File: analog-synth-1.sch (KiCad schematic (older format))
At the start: 49 parts, among them J1 CONN_02X08, J2 CONN_02X03, J3 CONN_02X02, Q1 2N3904, Q2 2N3904, Q3 2N3904, Q4 2N3906, Q5 2N3904, U1 LM741, U2 LM741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

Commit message: Change vco tuning system
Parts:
- added R17: 50k, symbol R
- added R6: 100k, symbol R
- RV3, RV4: value 100k -> 10k
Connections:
- wire segments 157 -> 158
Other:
- note removed: "Note: RV4's value\nshould be about\nhalf RV3's value."

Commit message: Move some wires around
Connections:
- wire segments 158 -> 204
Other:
- moved on the sheet: R6, RV3, RV4

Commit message: Add footprints and fix pin header orientation
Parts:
- added R7: 1k, Resistors_THT:R_Axial_DIN0207_L6.3mm_D2.5mm_P10.16mm_Horizontal, symbol R
- C1, C10, C11, C15, C2, C3, C4, C6, C7, C8: footprint (none) -> Capacitors_THT:C_Disc_D5.0mm_W2.5mm_P2.50mm
- C12, C13, C14: footprint (none) -> Capacitors_THT:CP_Radial_D6.3mm_P2.50mm
- C5: footprint (none) -> Capacitors_THT:C_Disc_D3.8mm_W2.6mm_P2.50mm
- C9: footprint (none) -> Capacitors_THT:C_Rect_L7.0mm_W3.5mm_P2.50mm_P5.00mm
- J1: footprint (none) -> Pin_Headers:Pin_Header_Straight_2x08_Pitch2.54mm
- J2: footprint (none) -> Pin_Headers:Pin_Header_Straight_2x03_Pitch2.54mm
- J3: footprint (none) -> Pin_Headers:Pin_Header_Straight_2x02_Pitch2.54mm
- Q1, Q2, Q3, Q4, Q5: footprint TO_SOT_Packages_THT:TO-92_Molded_Narrow -> TO_SOT_Packages_THT:TO-92_Inline_Wide
- R1, R2, R3, R4, R5: footprint (none) -> Resistors_THT:R_Axial_DIN0207_L6.3mm_D2.5mm_P10.16mm_Horizontal
- R10: renamed from R8; footprint (none) -> Resistors_THT:R_Axial_DIN0207_L6.3mm_D2.5mm_P10.16mm_Horizontal
- R11: renamed from R10; footprint (none) -> Resistors_THT:R_Axial_DIN0207_L6.3mm_D2.5mm_P10.16mm_Horizontal
- R12: renamed from R11; footprint (none) -> Resistors_THT:R_Axial_DIN0207_L6.3mm_D2.5mm_P10.16mm_Horizontal
- R13: renamed from R17; footprint (none) -> Resistors_THT:R_Axial_DIN0207_L6.3mm_D2.5mm_P10.16mm_Horizontal
- R14: renamed from R12; footprint (none) -> Resistors_THT:R_Axial_DIN0207_L6.3mm_D2.5mm_P10.16mm_Horizontal
- R15: renamed from R13; footprint (none) -> Resistors_THT:R_Axial_DIN0207_L6.3mm_D2.5mm_P10.16mm_Horizontal
- R16: renamed from R14; footprint (none) -> Resistors_THT:R_Axial_DIN0207_L6.3mm_D2.5mm_P10.16mm_Horizontal
- R17: renamed from R15; footprint (none) -> Resistors_THT:R_Axial_DIN0207_L6.3mm_D2.5mm_P10.16mm_Horizontal
- R18: renamed from R16; footprint (none) -> Resistors_THT:R_Axial_DIN0207_L6.3mm_D2.5mm_P10.16mm_Horizontal
- R6: renamed from R7; footprint (none) -> Resistors_THT:R_Axial_DIN0207_L6.3mm_D2.5mm_P10.16mm_Horizontal
- R8: renamed from R9; footprint (none) -> Resistors_THT:R_Axial_DIN0207_L6.3mm_D2.5mm_P10.16mm_Horizontal
- R9: renamed from R6; footprint (none) -> Resistors_THT:R_Axial_DIN0207_L6.3mm_D2.5mm_P10.16mm_Horizontal
- RV1, RV2, RV3, RV4: footprint (none) -> Potentiometers:Potentiometer_Trimmer_Bourns_3296Y
- U1, U2, U3, U4, U5, U6, U7: footprint (none) -> Housings_DIP:DIP-8_W7.62mm
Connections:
- wire segments 204 -> 158
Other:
- moved on the sheet: RV3

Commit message: Change trimmer descriptions and plot pdf
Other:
- note added: "RV1 is exponential product control.\nRV2 is product control.\nRV3 and RV4 are sum controls."
- note removed: "RV3 and RV4 are to try\nto compensate for C9's\nvalue."
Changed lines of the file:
@@
 Text Notes 1200 4500 0    60   ~ 0
 C9's value has a drastic\neffect on the VCO's frequency.
-Text Notes 1000 7350 0    60   ~ 0
-RV3 and RV4 are to try\nto compensate for C9's\nvalue.
 Wire Wire Line
 	2700 5800 2850 5800
@@
 Wire Wire Line
 	1500 4900 1500 5050
+Text Notes 3100 3800 0    60   ~ 0
+RV1 is exponential product control.\nRV2 is product control.\nRV3 and RV4 are sum controls.
 $EndSCHEMATC

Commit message: Use PJ301M-12 3.3mm jacks
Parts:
- removed J2: CONN_02X03, Pin_Headers:Pin_Header_Straight_2x03_Pitch2.54mm, symbol CONN_02X03
- removed J3: CONN_02X02, Pin_Headers:Pin_Header_Straight_2x02_Pitch2.54mm, symbol CONN_02X02
- removed R4, R6: 100k, Resistors_THT:R_Axial_DIN0207_L6.3mm_D2.5mm_P10.16mm_Horizontal, symbol R
- added J2, J3, J4: PJ301M-12, Eurocad:PJ301M-12, symbol PJ301M-12
- added RV5: POT, symbol POT
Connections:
- net labels removed: CV2, CV3
- wire segments 158 -> 156
- no-connect marks 14 -> 16
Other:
- note added: "Pitch control pot."
- moved on the sheet: C11, C12, C13, C14, C8, U4, U7

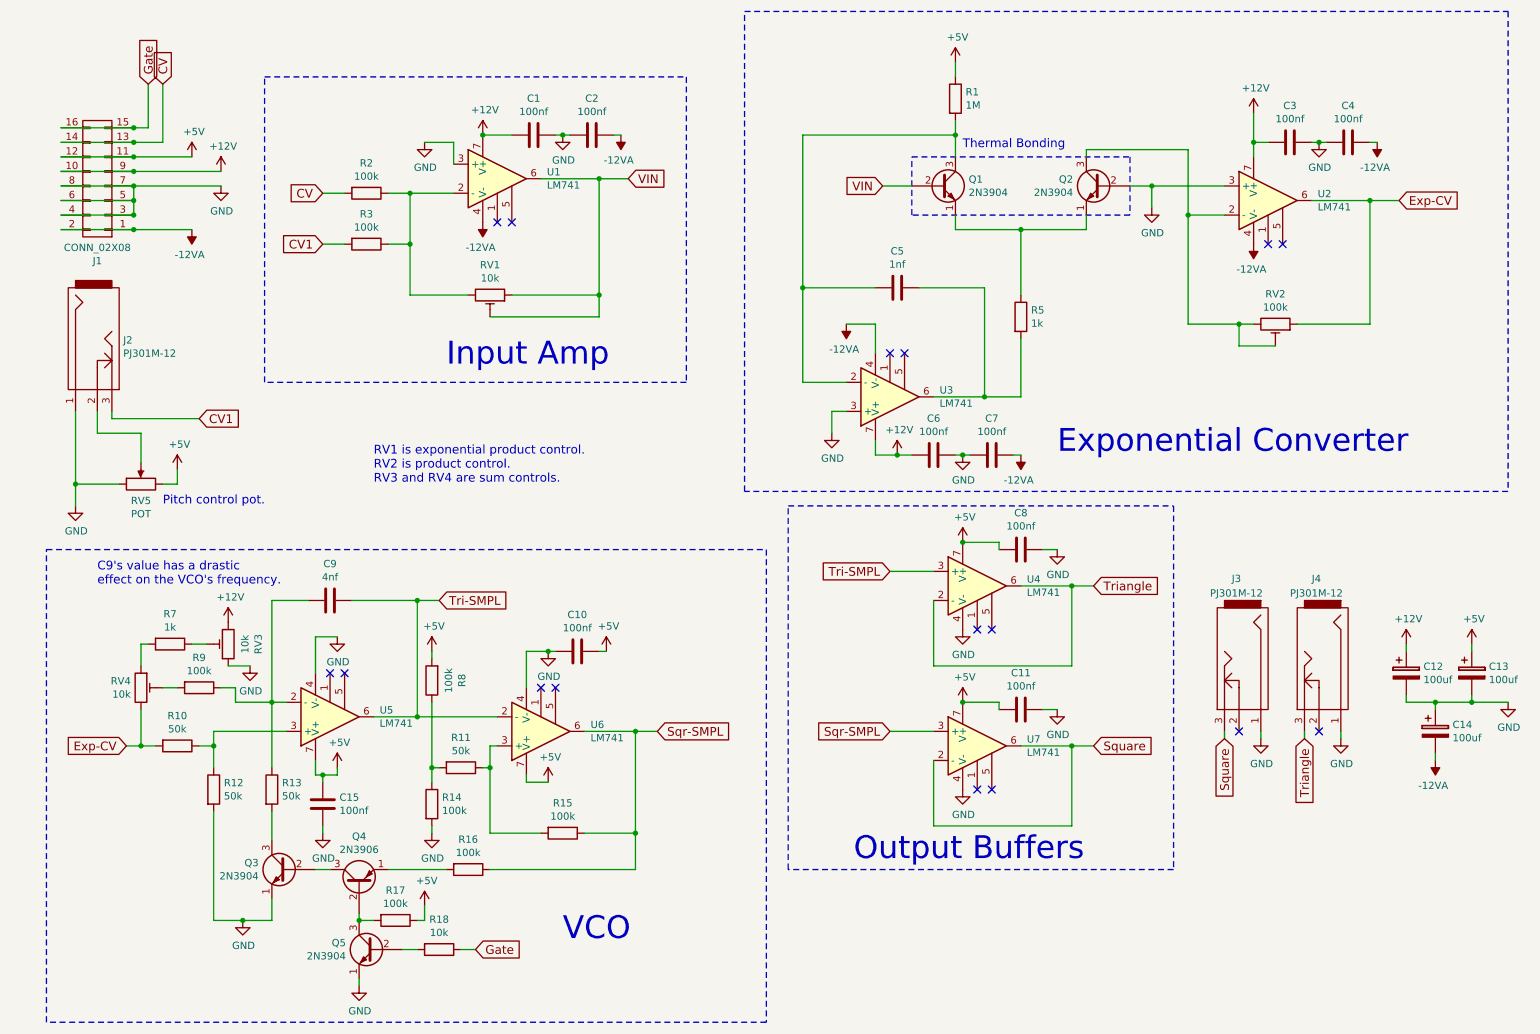
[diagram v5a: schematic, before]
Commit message: Update schematic libs, add Gate jack
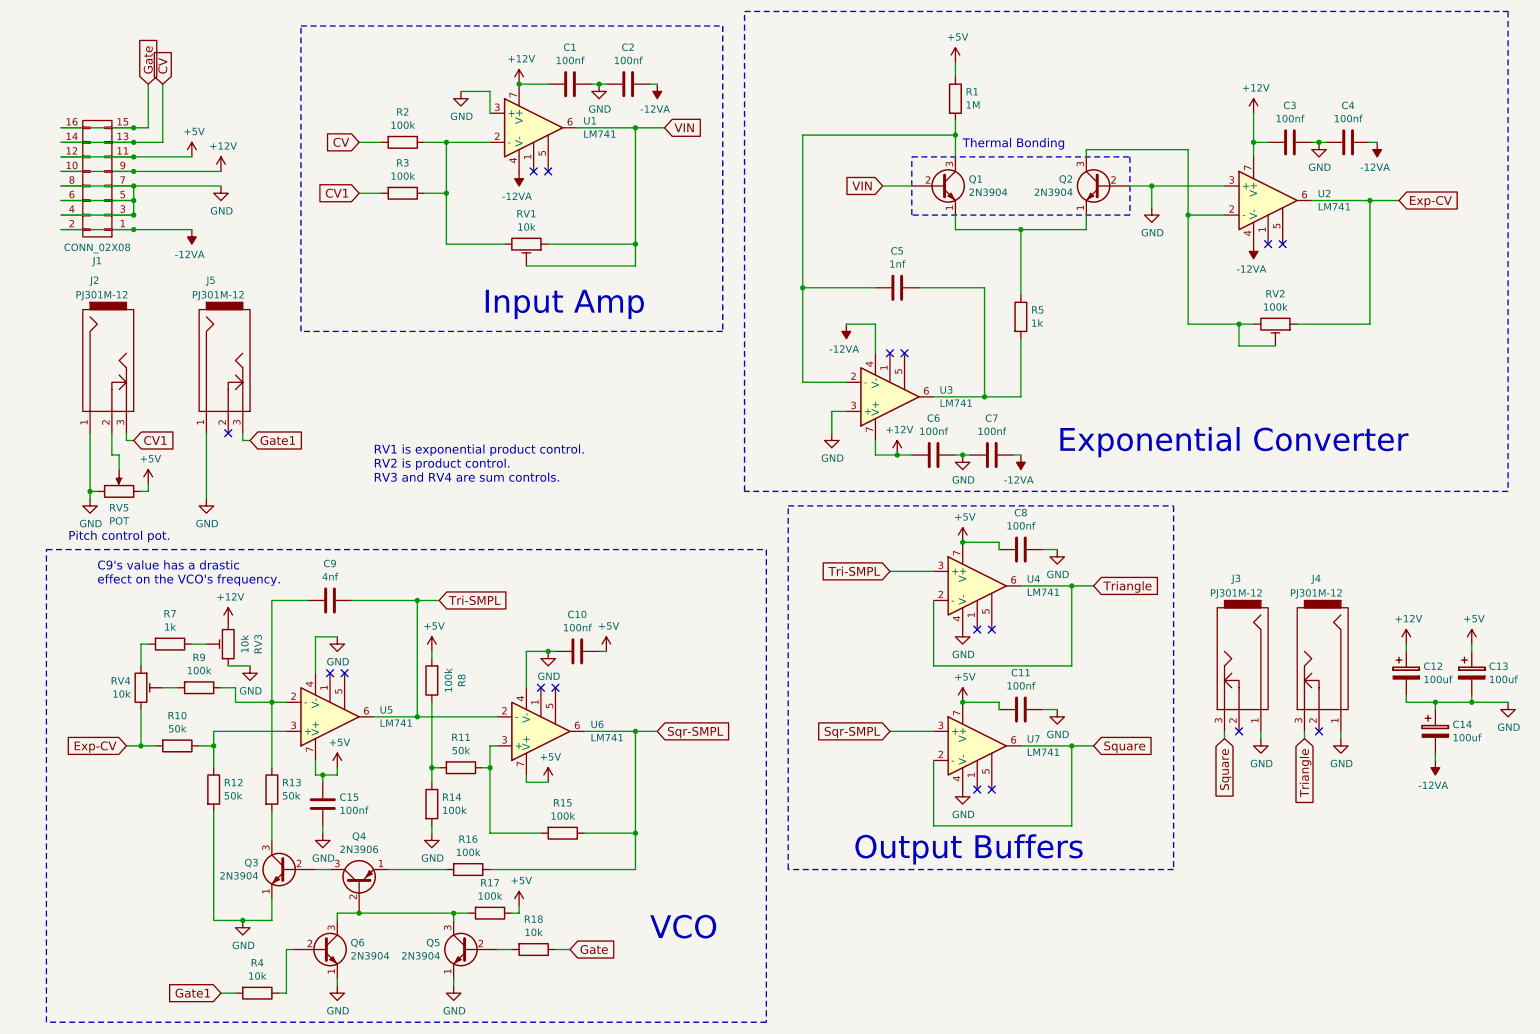
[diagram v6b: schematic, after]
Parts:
- added J5: PJ301M-12, Eurocad:PJ301M-12, symbol PJ301M-12
- added Q6: 2N3904, TO_SOT_Packages_THT:TO-92_Inline_Wide, symbol 2N3904
- added R4: 10k, Resistors_THT:R_Axial_DIN0207_L6.3mm_D2.5mm_P10.16mm_Horizontal, symbol R
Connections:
- net GND: now also J5.1, Q6.1 (E)
- net at Q4.2 (B), Q5.3 (C), R17.2: now also Q6.3 (C)
- new net: Q6.2 (B), R4.1
- new net Gate1: J5.3, R4.2
- no-connect marks 16 -> 17
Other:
- moved on the sheet: C1, C2, J2, Q5, R17, R18, R2, R3, RV1, RV5, U1

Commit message: Use RK09L potentiometer
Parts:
- RV5: footprint (none) -> Potentiometers:Potentiometer_Alps_RK09L_Sleve_Single_Horizontal
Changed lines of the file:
@@
 F 0 "RV5" V 1236 3850 50  0000 C CNN
 F 1 "POT" V 1145 3850 50  0000 C CNN
-F 2 "" H 1350 3850 50  0001 C CNN
+F 2 "Potentiometers:Potentiometer_Alps_RK09L_Sleve_Single_Horizontal" H 1350 3850 50  0001 C CNN
 F 3 "" H 1350 3850 50  0001 C CNN
 	1    1350 3850

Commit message: Begin on PCB
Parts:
- RV5: value POT -> 10k; footprint Potentiometers:Potentiometer_Alps_RK09L_Sleve_Single_Horizontal -> Potentiometers:Potentiometer_Alps_RK09L_Sleve_Single_Horizontal_Custom
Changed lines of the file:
@@
 P 1350 3850
 F 0 "RV5" V 1236 3850 50  0000 C CNN
-F 1 "POT" V 1145 3850 50  0000 C CNN
-F 2 "Potentiometers:Potentiometer_Alps_RK09L_Sleve_Single_Horizontal" H 1350 3850 50  0001 C CNN
+F 1 "10k" V 1145 3850 50  0000 C CNN
+F 2 "Potentiometers:Potentiometer_Alps_RK09L_Sleve_Single_Horizontal_Custom" H 1350 3850 50  0001 C CNN
 F 3 "" H 1350 3850 50  0001 C CNN
 	1    1350 3850
